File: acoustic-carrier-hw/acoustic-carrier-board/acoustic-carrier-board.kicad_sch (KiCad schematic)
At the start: 0 parts

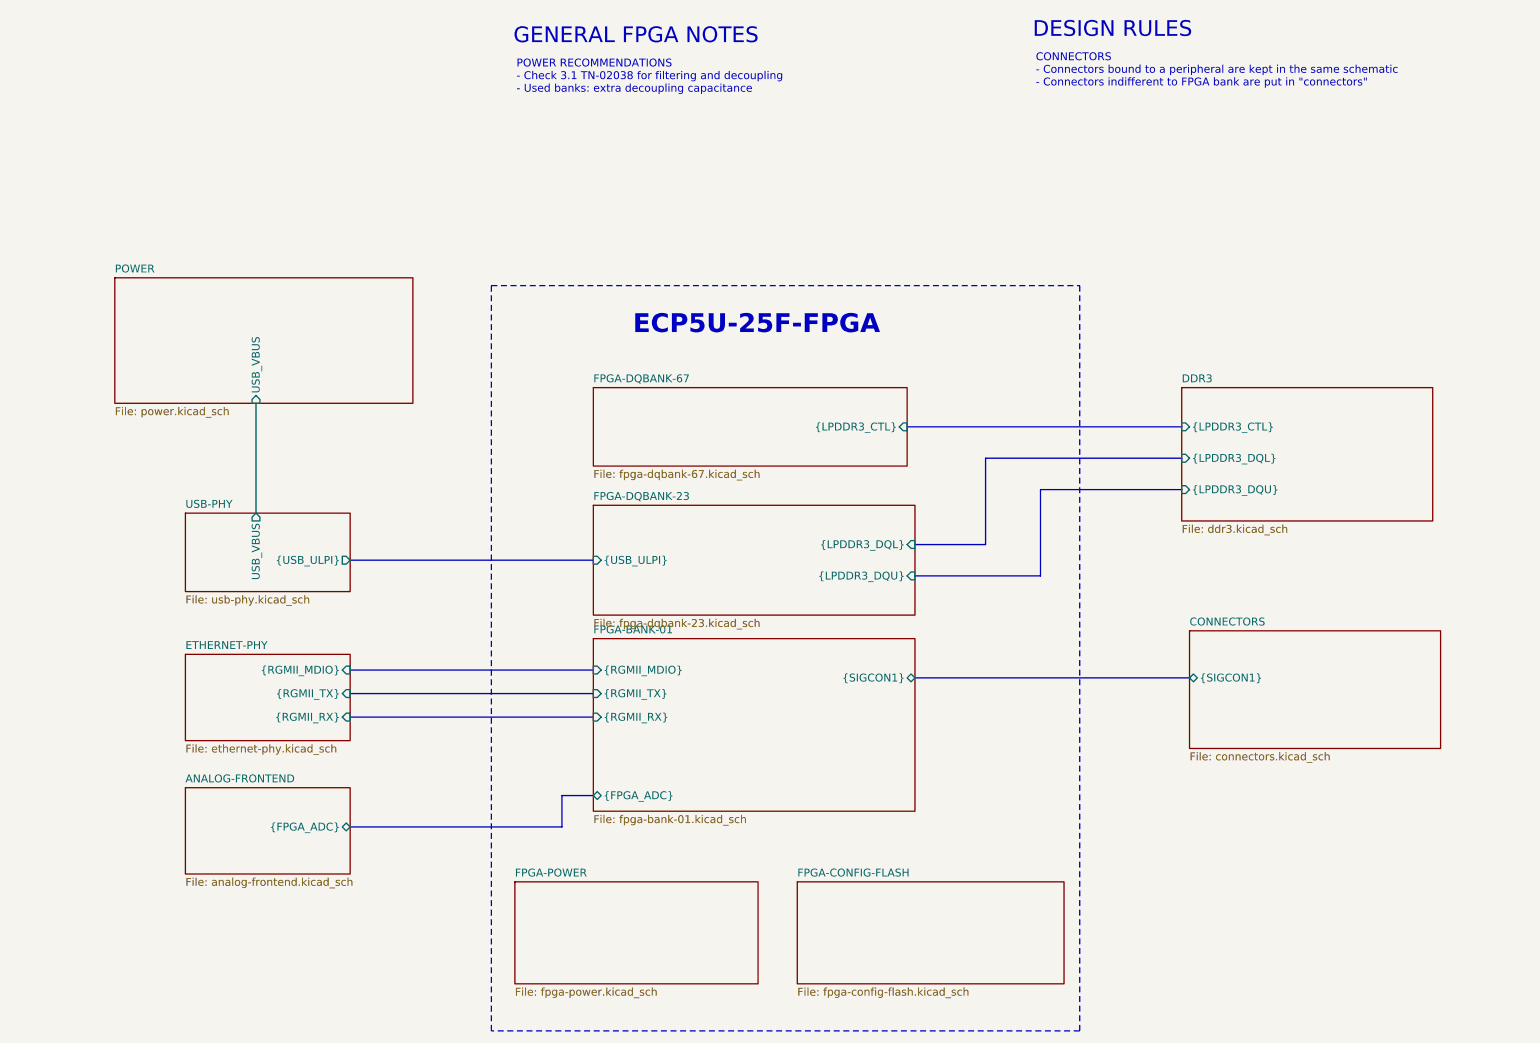
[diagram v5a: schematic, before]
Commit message: [carrier] Added testpoints
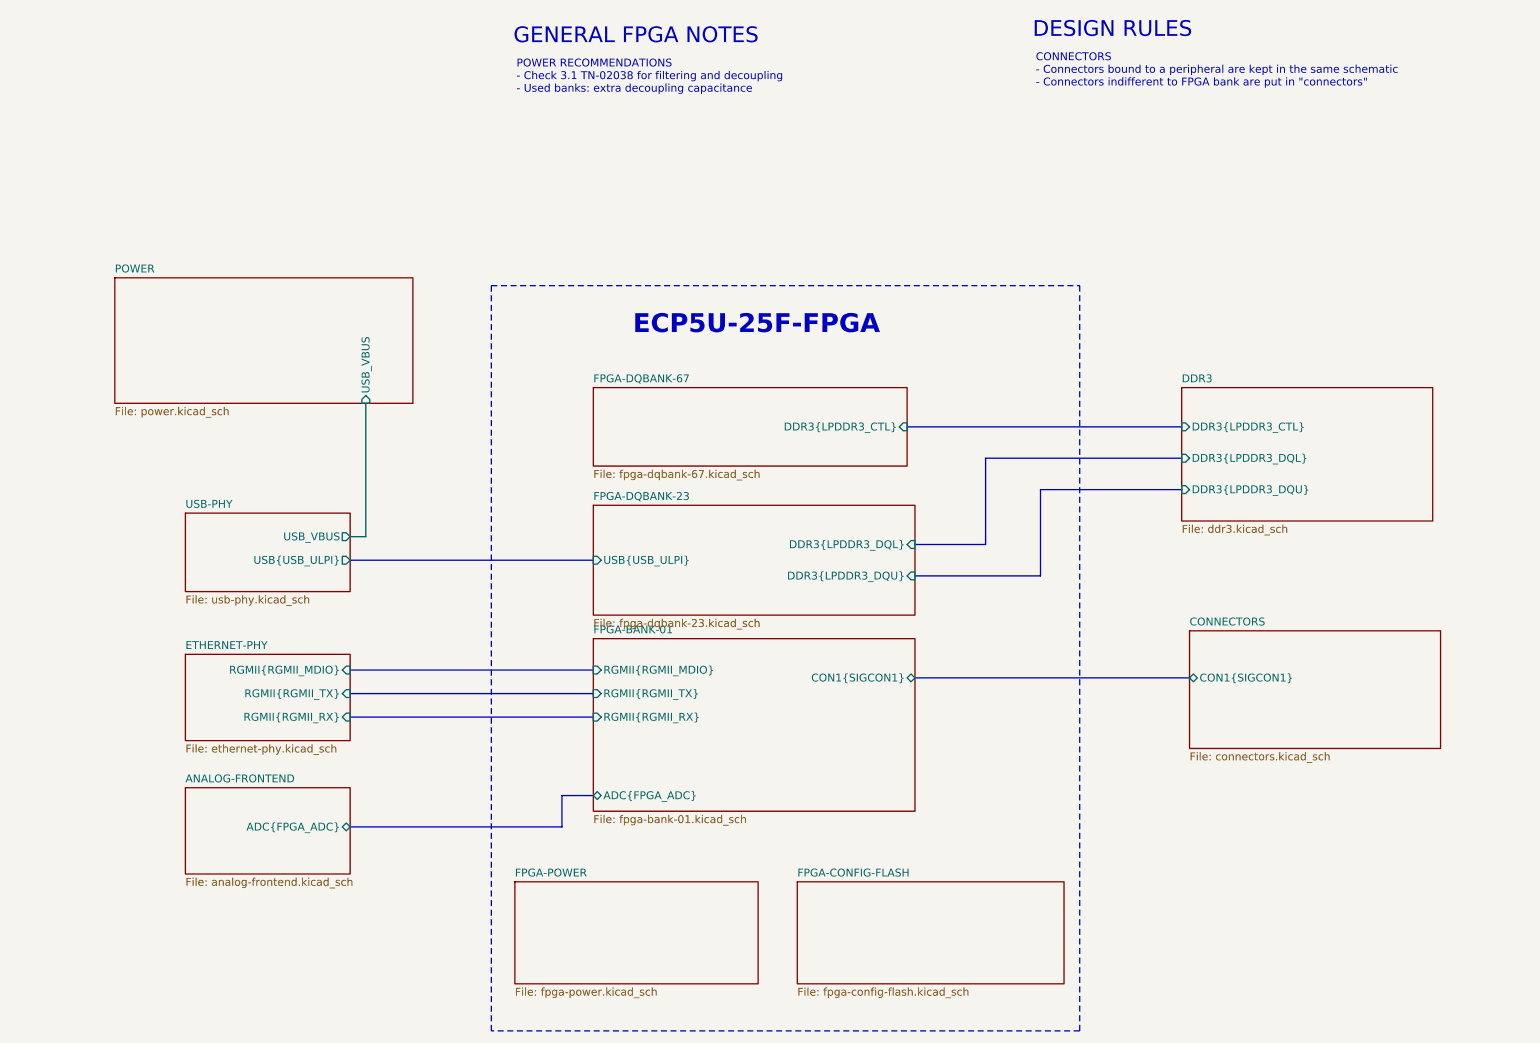
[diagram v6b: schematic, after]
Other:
- sheet ANALOG-FRONTEND ports: added ADC{FPGA_ADC}; removed {FPGA_ADC}
- sheet CONNECTORS ports: added CON1{SIGCON1}; removed {SIGCON1}
- sheet DDR3 ports: added DDR3{LPDDR3_CTL}, DDR3{LPDDR3_DQL}, DDR3{LPDDR3_DQU}; removed {LPDDR3_CTL}, {LPDDR3_DQL}, {LPDDR3_DQU}
- sheet ETHERNET-PHY ports: added RGMII{RGMII_MDIO}, RGMII{RGMII_RX}, RGMII{RGMII_TX}; removed {RGMII_MDIO}, {RGMII_RX}, {RGMII_TX}
- sheet FPGA-BANK-01 ports: added ADC{FPGA_ADC}, CON1{SIGCON1}, RGMII{RGMII_MDIO}, RGMII{RGMII_RX}, RGMII{RGMII_TX}; removed {FPGA_ADC}, {RGMII_MDIO}, {RGMII_RX}, {RGMII_TX}, {SIGCON1}
- sheet FPGA-DQBANK-23 ports: added DDR3{LPDDR3_DQL}, DDR3{LPDDR3_DQU}, USB{USB_ULPI}; removed {LPDDR3_DQL}, {LPDDR3_DQU}, {USB_ULPI}
- sheet FPGA-DQBANK-67 ports: added DDR3{LPDDR3_CTL}; removed {LPDDR3_CTL}
- sheet USB-PHY ports: added USB{USB_ULPI}; removed {USB_ULPI}
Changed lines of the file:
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@@
 	(wire
 		(pts
-			(xy 62.23 48.26) (xy 62.23 66.04)
+			(xy 77.47 69.85) (xy 80.01 69.85)
 		)
 		(stroke
@@
 		(pts
 			(xy 77.47 73.66) (xy 116.84 73.66)
+		)
+		(stroke
+			(width 0)
+			(type default)
+		)
+	)
+	(wire
+		(pts
+			(xy 80.01 48.26) (xy 80.01 69.85)
 		)
 		(stroke
@@
 		)
 		(pin "USB_VBUS" input
-			(at 62.23 48.26 270)
+			(at 80.01 48.26 270)
 			(effects
 				(font
@@
 			)
 		)
-		(pin "{RGMII_RX}" input
+		(pin "RGMII{RGMII_RX}" input
 			(at 116.84 99.06 180)
 			(effects
@@
 			)
 		)
-		(pin "{RGMII_MDIO}" input
+		(pin "RGMII{RGMII_MDIO}" input
 			(at 116.84 91.44 180)
 			(effects
@@
 			)
 		)
-		(pin "{FPGA_ADC}" bidirectional
+		(pin "ADC{FPGA_ADC}" bidirectional
 			(at 116.84 111.76 180)
 			(effects
@@
 			)
 		)
-		(pin "{RGMII_TX}" input
+		(pin "RGMII{RGMII_TX}" input
 			(at 116.84 95.25 180)
 			(effects
@@
 			)
 		)
-		(pin "{SIGCON1}" bidirectional
+		(pin "CON1{SIGCON1}" bidirectional
 			(at 168.91 92.71 0)
 			(effects
@@
 			)
 		)
-		(pin "{FPGA_ADC}" bidirectional
+		(pin "ADC{FPGA_ADC}" bidirectional
 			(at 77.47 116.84 0)
 			(effects
@@
 			)
 		)
-		(pin "{LPDDR3_CTL}" input
+		(pin "DDR3{LPDDR3_CTL}" input
 			(at 167.64 52.07 0)
 			(effects
@@
 			)
 		)
-		(pin "{USB_ULPI}" input
+		(pin "USB{USB_ULPI}" input
 			(at 116.84 73.66 180)
 			(effects
@@
 			)
 		)
-		(pin "{LPDDR3_DQL}" input
+		(pin "DDR3{LPDDR3_DQL}" input
 			(at 168.91 71.12 0)
 			(effects
@@
 			)
 		)
-		(pin "{LPDDR3_DQU}" input
+		(pin "DDR3{LPDDR3_DQU}" input
 			(at 168.91 76.2 0)
 			(effects
@@
 			)
 		)
-		(pin "{SIGCON1}" bidirectional
+		(pin "CON1{SIGCON1}" bidirectional
 			(at 213.36 92.71 180)
 			(effects
@@
 			)
 		)
-		(pin "{USB_ULPI}" output
+		(pin "USB{USB_ULPI}" output
 			(at 77.47 73.66 0)
 			(effects
@@
 		)
 		(pin "USB_VBUS" output
-			(at 62.23 66.04 90)
+			(at 77.47 69.85 0)
 			(effects
 				(font
@@
 			)
 		)
-		(pin "{RGMII_TX}" input
+		(pin "RGMII{RGMII_TX}" input
 			(at 77.47 95.25 0)
 			(effects
@@
 			)
 		)
-		(pin "{RGMII_RX}" input
+		(pin "RGMII{RGMII_RX}" input
 			(at 77.47 99.06 0)
 			(effects
@@
 			)
 		)
-		(pin "{RGMII_MDIO}" input
+		(pin "RGMII{RGMII_MDIO}" input
 			(at 77.47 91.44 0)
 			(effects
@@
 			)
 		)
-		(pin "{LPDDR3_DQU}" input
+		(pin "DDR3{LPDDR3_DQU}" input
 			(at 212.09 62.23 180)
 			(effects
@@
 			)
 		)
-		(pin "{LPDDR3_CTL}" input
+		(pin "DDR3{LPDDR3_CTL}" input
 			(at 212.09 52.07 180)
 			(effects
@@
 			)
 		)
-		(pin "{LPDDR3_DQL}" input
+		(pin "DDR3{LPDDR3_DQL}" input
 			(at 212.09 57.15 180)
 			(effects

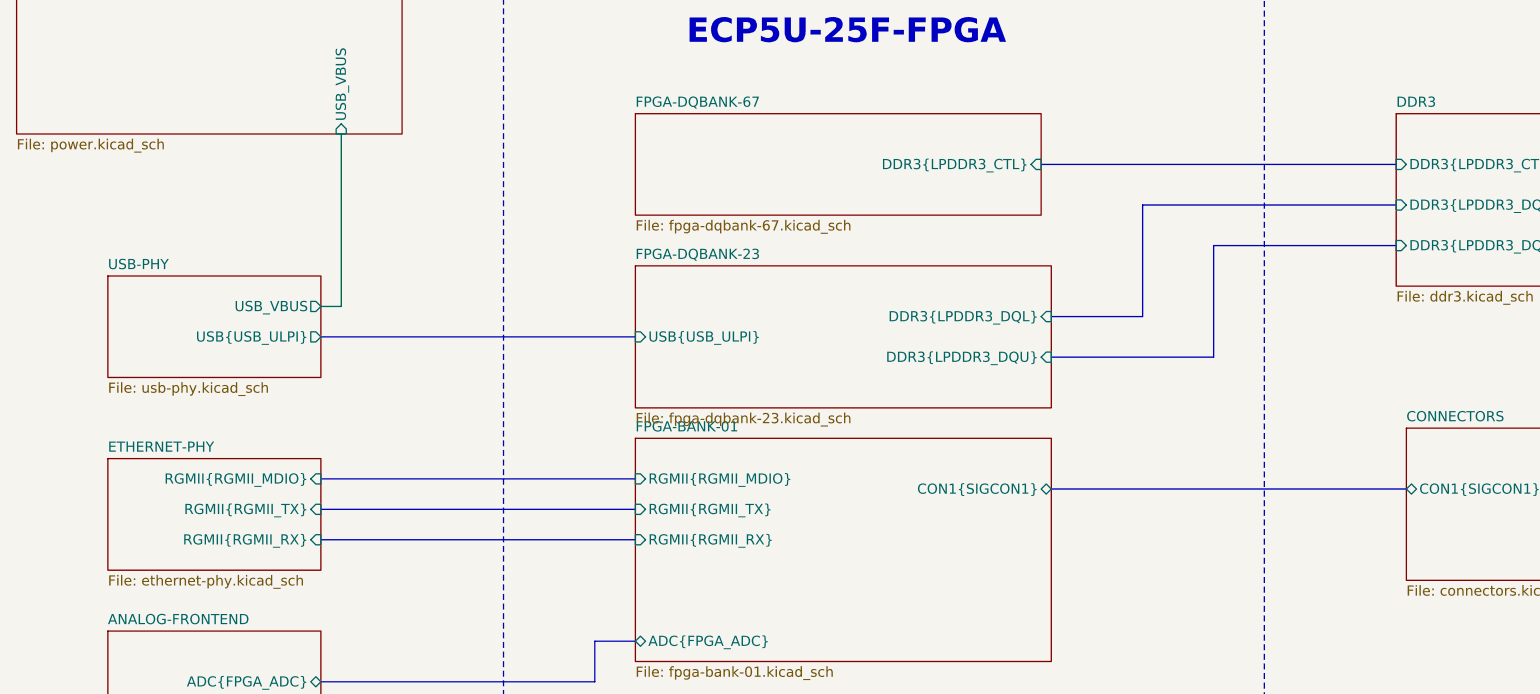
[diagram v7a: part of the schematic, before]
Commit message: [carrier] Removed USB-switch, placed decouplpling for DDR3 and ECP5U (next) consider adding buffers on CC1 and CC2 pins
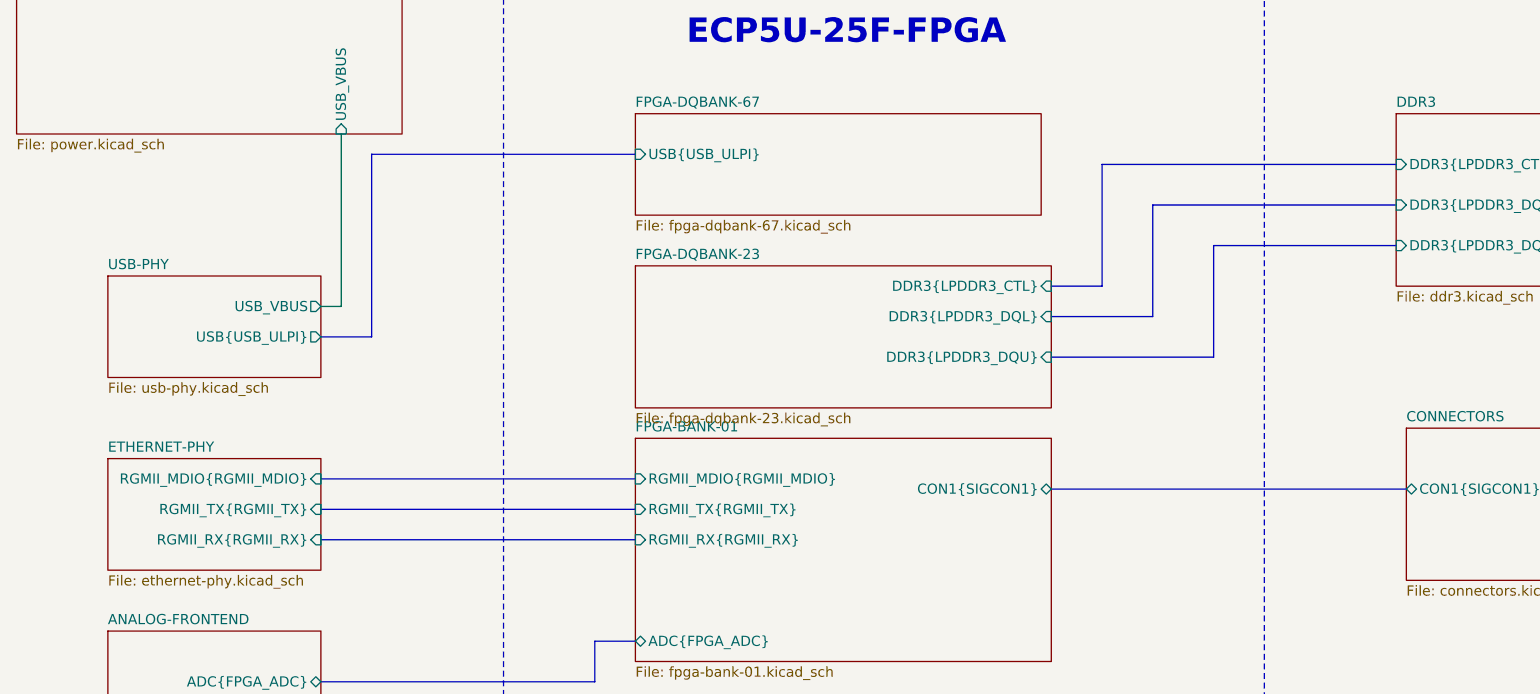
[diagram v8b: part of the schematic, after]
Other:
- sheet ETHERNET-PHY ports: added RGMII_MDIO{RGMII_MDIO}, RGMII_RX{RGMII_RX}, RGMII_TX{RGMII_TX}; removed RGMII{RGMII_MDIO}, RGMII{RGMII_RX}, RGMII{RGMII_TX}
- sheet FPGA-BANK-01 ports: added RGMII_MDIO{RGMII_MDIO}, RGMII_RX{RGMII_RX}, RGMII_TX{RGMII_TX}; removed RGMII{RGMII_MDIO}, RGMII{RGMII_RX}, RGMII{RGMII_TX}
- sheet FPGA-DQBANK-23 ports: added DDR3{LPDDR3_CTL}; removed USB{USB_ULPI}
- sheet FPGA-DQBANK-67 ports: added USB{USB_ULPI}; removed DDR3{LPDDR3_CTL}
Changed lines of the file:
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@@
 	(bus
 		(pts
-			(xy 180.34 57.15) (xy 212.09 57.15)
+			(xy 175.26 52.07) (xy 212.09 52.07)
+		)
+		(stroke
+			(width 0)
+			(type default)
+		)
+	)
+	(bus
+		(pts
+			(xy 181.61 57.15) (xy 212.09 57.15)
 		)
 		(stroke
@@
 	(bus
 		(pts
-			(xy 77.47 73.66) (xy 116.84 73.66)
+			(xy 116.84 50.8) (xy 83.82 50.8)
 		)
 		(stroke
@@
 	(bus
 		(pts
-			(xy 167.64 52.07) (xy 212.09 52.07)
-		)
-		(stroke
-			(width 0)
-			(type default)
-		)
-	)
-	(bus
-		(pts
 			(xy 189.23 76.2) (xy 168.91 76.2)
 		)
@@
 	(bus
 		(pts
-			(xy 180.34 57.15) (xy 180.34 71.12)
+			(xy 181.61 57.15) (xy 181.61 71.12)
+		)
+		(stroke
+			(width 0)
+			(type default)
+		)
+	)
+	(bus
+		(pts
+			(xy 83.82 50.8) (xy 83.82 73.66)
 		)
 		(stroke
@@
 	(bus
 		(pts
+			(xy 168.91 67.31) (xy 175.26 67.31)
+		)
+		(stroke
+			(width 0)
+			(type default)
+		)
+	)
+	(bus
+		(pts
 			(xy 168.91 92.71) (xy 213.36 92.71)
 		)
@@
 	(bus
 		(pts
+			(xy 83.82 73.66) (xy 77.47 73.66)
+		)
+		(stroke
+			(width 0)
+			(type default)
+		)
+	)
+	(bus
+		(pts
+			(xy 175.26 67.31) (xy 175.26 52.07)
+		)
+		(stroke
+			(width 0)
+			(type default)
+		)
+	)
+	(bus
+		(pts
 			(xy 77.47 99.06) (xy 116.84 99.06)
 		)
@@
 	(bus
 		(pts
-			(xy 180.34 71.12) (xy 168.91 71.12)
+			(xy 181.61 71.12) (xy 168.91 71.12)
 		)
 		(stroke
@@
 			)
 		)
-		(pin "RGMII{RGMII_RX}" input
+		(pin "RGMII_RX{RGMII_RX}" input
 			(at 116.84 99.06 180)
 			(effects
@@
 			)
 		)
-		(pin "RGMII{RGMII_MDIO}" input
+		(pin "RGMII_MDIO{RGMII_MDIO}" input
 			(at 116.84 91.44 180)
 			(effects
@@
 			)
 		)
-		(pin "RGMII{RGMII_TX}" input
+		(pin "RGMII_TX{RGMII_TX}" input
 			(at 116.84 95.25 180)
 			(effects
@@
 			)
 		)
-		(pin "DDR3{LPDDR3_CTL}" input
-			(at 167.64 52.07 0)
-			(effects
-				(font
-					(size 1.27 1.27)
-				)
-				(justify right)
+		(pin "USB{USB_ULPI}" input
+			(at 116.84 50.8 180)
+			(effects
+				(font
+					(size 1.27 1.27)
+				)
+				(justify left)
 			)
 		)
@@
 			)
 		)
-		(pin "USB{USB_ULPI}" input
-			(at 116.84 73.66 180)
-			(effects
-				(font
-					(size 1.27 1.27)
-				)
-				(justify left)
-			)
-		)
 		(pin "DDR3{LPDDR3_DQL}" input
 			(at 168.91 71.12 0)
@@
 			)
 		)
+		(pin "DDR3{LPDDR3_CTL}" input
+			(at 168.91 67.31 0)
+			(effects
+				(font
+					(size 1.27 1.27)
+				)
+				(justify right)
+			)
+		)
 		(instances
 			(project "acoustic-carrier-board"
@@
 			)
 		)
-		(pin "RGMII{RGMII_TX}" input
+		(pin "RGMII_TX{RGMII_TX}" input
 			(at 77.47 95.25 0)
 			(effects
@@
 			)
 		)
-		(pin "RGMII{RGMII_RX}" input
+		(pin "RGMII_RX{RGMII_RX}" input
 			(at 77.47 99.06 0)
 			(effects
@@
 			)
 		)
-		(pin "RGMII{RGMII_MDIO}" input
+		(pin "RGMII_MDIO{RGMII_MDIO}" input
 			(at 77.47 91.44 0)
 			(effects
